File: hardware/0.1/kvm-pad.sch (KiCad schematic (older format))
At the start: 50 parts, among them J1 USB_C_Receptacle_USB2.0, J2 USB_C_Receptacle_USB2.0, J3 AVR-ISP-6, K1 KEYSW, K2 KEYSW, K3 KEYSW, K4 KEYSW, K5 KEYSW, K6 KEYSW, K7 KEYSW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

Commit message: [sch][pcb] Swap USBLC6 IOs for easing PCB routing
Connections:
- net 1_D+: now also U1.1 (IO1); no longer U1.3 (IO2)
- net 1_D-: now also U1.3 (IO2); no longer U1.1 (IO1)
- net 2_D+: now also U3.1 (IO1); no longer U3.3 (IO2)
- net 2_D-: now also U3.3 (IO2); no longer U3.1 (IO1)
- net USB_1_D+: now also U1.6 (IO1); no longer U1.4 (IO2)
- net USB_1_D-: now also U1.4 (IO2); no longer U1.6 (IO1)
- net USB_2_D+: now also U3.6 (IO1); no longer U3.4 (IO2)
- net USB_2_D-: now also U3.4 (IO2); no longer U3.6 (IO1)
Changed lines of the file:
@@
 	1700 1950 1650 1950
 Wire Wire Line
-	1700 1700 2150 1700
+	1700 1700 2150 1900
 Connection ~ 1700 1700
 Wire Wire Line
 	1700 1700 1700 1750
-Text Label 2150 1700 2    50   ~ 0
+Text Label 2150 1900 2    50   ~ 0
 1_D-
 Wire Wire Line
-	1700 1900 2150 1900
+	1700 1900 2150 1700
 Connection ~ 1700 1900
 Wire Wire Line
@@
 	1650 4100 1700 4100
 Wire Wire Line
-	1700 4100 1700 4150
-Wire Wire Line
 	1700 4200 1650 4200
 Wire Wire Line
-	1700 3950 2150 3950
+	1700 3950 2150 4150
 Connection ~ 1700 3950
 Wire Wire Line
 	1700 3950 1700 4000
-Wire Wire Line
-	1700 4150 2150 4150
-Connection ~ 1700 4150
-Wire Wire Line
-	1700 4150 1700 4200
 $Comp
 L josh-passive:RN RN?
@@
 	1    0    0    -1
 $EndComp
-Text Label 2150 1900 2    50   ~ 0
+Text Label 2150 1700 2    50   ~ 0
 1_D+
+Text Label 2150 3950 2    50   ~ 0
+2_D+
 Text Label 2150 4150 2    50   ~ 0
-2_D+
-Text Label 2150 3950 2    50   ~ 0
 2_D-
 $Comp
@@
 Wire Wire Line
 	2350 1150 2550 1150
+Text Label 3400 1700 2    50   ~ 0
+USB_1_D+
+Wire Wire Line
+	2950 1900 3400 1900
 Text Label 3400 1900 2    50   ~ 0
-USB_1_D+
-Wire Wire Line
-	2950 1900 3400 1900
-Text Label 3400 1700 2    50   ~ 0
 USB_1_D-
 Wire Wire Line
@@
 Wire Wire Line
 	2950 4150 3400 4150
+Text Label 3400 3950 2    50   ~ 0
+USB_2_D+
 Text Label 3400 4150 2    50   ~ 0
-USB_2_D+
-Text Label 3400 3950 2    50   ~ 0
 USB_2_D-
 Text Notes 1100 5525 0    100  ~ 0
@@
 	1    0    0    -1
 $EndComp
+Wire Wire Line
+	1700 4100 1700 4150
+Wire Wire Line
+	1700 4150 2150 3950
+Connection ~ 1700 4150
+Wire Wire Line
+	1700 4150 1700 4200
 $EndSCHEMATC

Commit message: [pcb] Switch RN1 to 4xR
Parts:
- R17, R18, R19, R20: renamed from RN1; footprint Resistor_SMD:R_Array_Convex_4x0603 -> Resistor_SMD:R_0603_1608Metric; symbol josh-passive:RN -> Device:R
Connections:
- net GND: now also R17.1, R18.1, R19.1, R20.1; no longer R17.5, R18.6, R19.7, R20.8
- net at J1.A5 (CC1): now also R17.2; no longer R17.4
- net at J1.B5 (CC2): now also R18.2; no longer R18.3
- net at J2.B5 (CC2): now also R20.2; no longer R20.1
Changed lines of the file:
@@
 	0    1    1    0
-$EndComp
-$Comp
-L josh-passive:RN RN?
-U 1 1 603A219F
-P 1850 1350
-AR Path="/5EDC3803/603A219F" Ref="RN?"  Part="1"
-AR Path="/603A219F" Ref="RN1"  Part="1"
-F 0 "RN1" H 1850 1450 50  0000 C CNN
-F 1 "5K1" H 1850 1350 50  0000 C CNN
-F 2 "Resistor_SMD:R_Array_Convex_4x0603" V 1850 1350 50  0001 C CNN
-F 3 "~" V 1850 1350 50  0001 C CNN
-	1    1850 1350
-	1    0    0    -1
-$EndComp
-$Comp
-L josh-passive:RN RN?
-U 2 1 603A21A5
-P 1850 1450
-AR Path="/5EDC3803/603A21A5" Ref="RN?"  Part="2"
-AR Path="/603A21A5" Ref="RN1"  Part="2"
-F 0 "RN1" H 1850 1350 50  0000 C CNN
-F 1 "5K1" H 1850 1450 50  0000 C CNN
-F 2 "Resistor_SMD:R_Array_Convex_4x0603" V 1850 1450 50  0001 C CNN
-F 3 "~" V 1850 1450 50  0001 C CNN
-	2    1850 1450
-	1    0    0    -1
 $EndComp
 Wire Wire Line
@@
 Wire Wire Line
 	1700 3950 1700 4000
-$Comp
-L josh-passive:RN RN?
-U 3 1 603A21FB
-P 1850 3600
-AR Path="/5EDC3803/603A21FB" Ref="RN?"  Part="3"
-AR Path="/603A21FB" Ref="RN1"  Part="3"
-F 0 "RN1" H 1850 3700 50  0000 C CNN
-F 1 "5K1" H 1850 3600 50  0000 C CNN
-F 2 "Resistor_SMD:R_Array_Convex_4x0603" V 1850 3600 50  0001 C CNN
-F 3 "~" V 1850 3600 50  0001 C CNN
-	3    1850 3600
-	1    0    0    -1
-$EndComp
-$Comp
-L josh-passive:RN RN?
-U 4 1 603A2201
-P 1850 3700
-AR Path="/5EDC3803/603A2201" Ref="RN?"  Part="4"
-AR Path="/603A2201" Ref="RN1"  Part="4"
-F 0 "RN1" H 1850 3600 50  0000 C CNN
-F 1 "5K1" H 1850 3700 50  0000 C CNN
-F 2 "Resistor_SMD:R_Array_Convex_4x0603" V 1850 3700 50  0001 C CNN
-F 3 "~" V 1850 3700 50  0001 C CNN
-	4    1850 3700
-	1    0    0    -1
-$EndComp
 Wire Wire Line
 	1700 3700 1650 3700
-Wire Wire Line
-	1650 3600 1700 3600
 Wire Wire Line
 	2000 3600 2050 3600
@@
 Text Notes 1100 5525 0    100  ~ 0
 USB Switch and Hub
-$Comp
-L Connector:USB_C_Receptacle_USB2.0 J?
-U 1 1 603A2178
-P 1050 1750
-AR Path="/5EDC3803/603A2178" Ref="J?"  Part="1"
-AR Path="/603A2178" Ref="J1"  Part="1"
-F 0 "J1" H 1157 2617 50  0000 C CNN
-F 1 "USB_C_Receptacle_USB2.0" H 1157 2526 50  0000 C CNN
-F 2 "josh-connectors:USB_C_U262-161N-4BVC11" H 1200 1750 50  0001 C CNN
-F 3 "https://www.usb.org/sites/default/files/documents/usb_type-c.zip" H 1200 1750 50  0001 C CNN
-	1    1050 1750
-	1    0    0    -1
-$EndComp
 $Comp
 L Connector:USB_C_Receptacle_USB2.0 J?
@@
 Wire Wire Line
 	1700 4150 1700 4200
+$Comp
+L Connector:USB_C_Receptacle_USB2.0 J?
+U 1 1 603A2178
+P 1050 1750
+AR Path="/5EDC3803/603A2178" Ref="J?"  Part="1"
+AR Path="/603A2178" Ref="J1"  Part="1"
+F 0 "J1" H 1157 2617 50  0000 C CNN
+F 1 "USB_C_Receptacle_USB2.0" H 1157 2526 50  0000 C CNN
+F 2 "josh-connectors:USB_C_U262-161N-4BVC11" H 1200 1750 50  0001 C CNN
+F 3 "https://www.usb.org/sites/default/files/documents/usb_type-c.zip" H 1200 1750 50  0001 C CNN
+	1    1050 1750
+	1    0    0    -1
+$EndComp
+Wire Wire Line
+	1650 3600 1700 3600
+$Comp
+L Device:R RN?
+U 1 1 603A2201
+P 1850 3700
+AR Path="/5EDC3803/603A2201" Ref="RN?"  Part="4"
+AR Path="/603A2201" Ref="R20"  Part="1"
+F 0 "R20" V 1950 3700 50  0000 C CNN
+F 1 "5K1" V 1850 3700 50  0000 C CNN
+F 2 "Resistor_SMD:R_0603_1608Metric" V 1850 3700 50  0001 C CNN
+F 3 "~" V 1850 3700 50  0001 C CNN
+	1    1850 3700
+	0    1    1    0
+$EndComp
+$Comp
+L Device:R RN?
+U 1 1 603A21A5
+P 1850 1450
+AR Path="/5EDC3803/603A21A5" Ref="RN?"  Part="2"
+AR Path="/603A21A5" Ref="R18"  Part="1"
+F 0 "R18" V 1950 1450 50  0000 C CNN
+F 1 "5K1" V 1850 1450 50  0000 C CNN
+F 2 "Resistor_SMD:R_0603_1608Metric" V 1850 1450 50  0001 C CNN
+F 3 "~" V 1850 1450 50  0001 C CNN
+	1    1850 1450
+	0    1    1    0
+$EndComp
+$Comp
+L Device:R RN?
+U 1 1 603A219F
+P 1850 1350
+AR Path="/5EDC3803/603A219F" Ref="RN?"  Part="1"
+AR Path="/603A219F" Ref="R17"  Part="1"
+F 0 "R17" V 1750 1350 50  0000 C CNN
+F 1 "5K1" V 1850 1350 50  0000 C CNN
+F 2 "Resistor_SMD:R_0603_1608Metric" V 1850 1350 50  0001 C CNN
+F 3 "~" V 1850 1350 50  0001 C CNN
+	1    1850 1350
+	0    1    1    0
+$EndComp
+$Comp
+L Device:R RN?
+U 1 1 603A21FB
+P 1850 3600
+AR Path="/5EDC3803/603A21FB" Ref="RN?"  Part="3"
+AR Path="/603A21FB" Ref="R19"  Part="1"
+F 0 "R19" V 1750 3600 50  0000 C CNN
+F 1 "5K1" V 1850 3600 50  0000 C CNN
+F 2 "Resistor_SMD:R_0603_1608Metric" V 1850 3600 50  0001 C CNN
+F 3 "~" V 1850 3600 50  0001 C CNN
+	1    1850 3600
+	0    1    1    0
+$EndComp
 $EndSCHEMATC

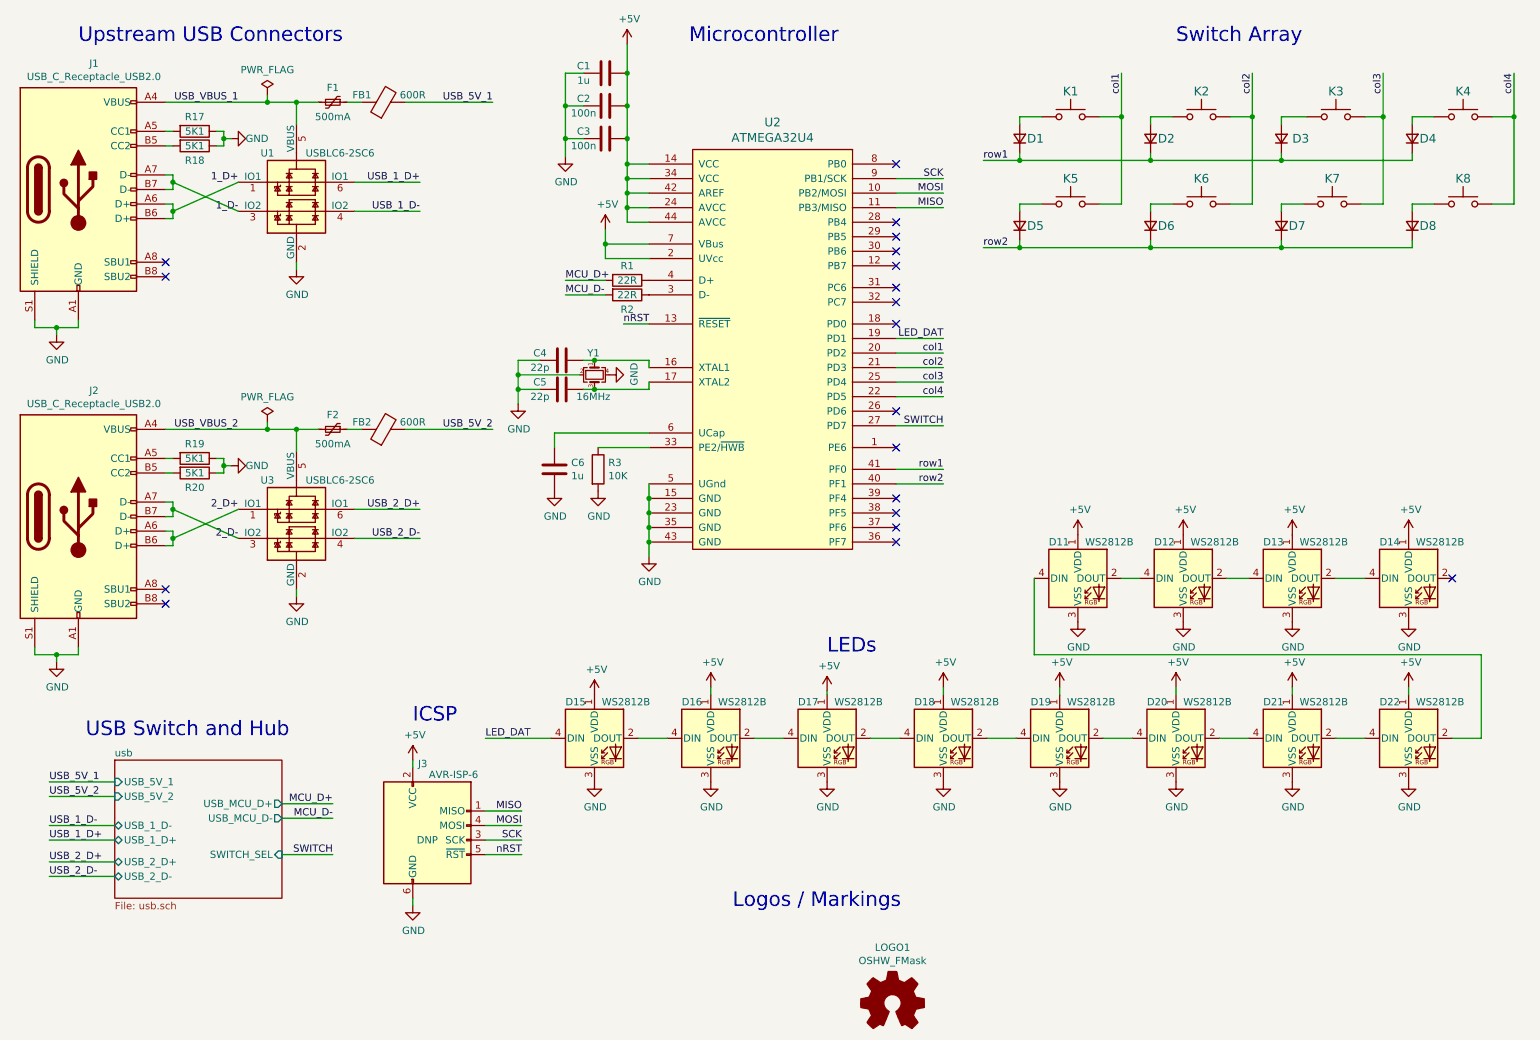
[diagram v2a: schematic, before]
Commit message: alt layout
following what usb says... ;p
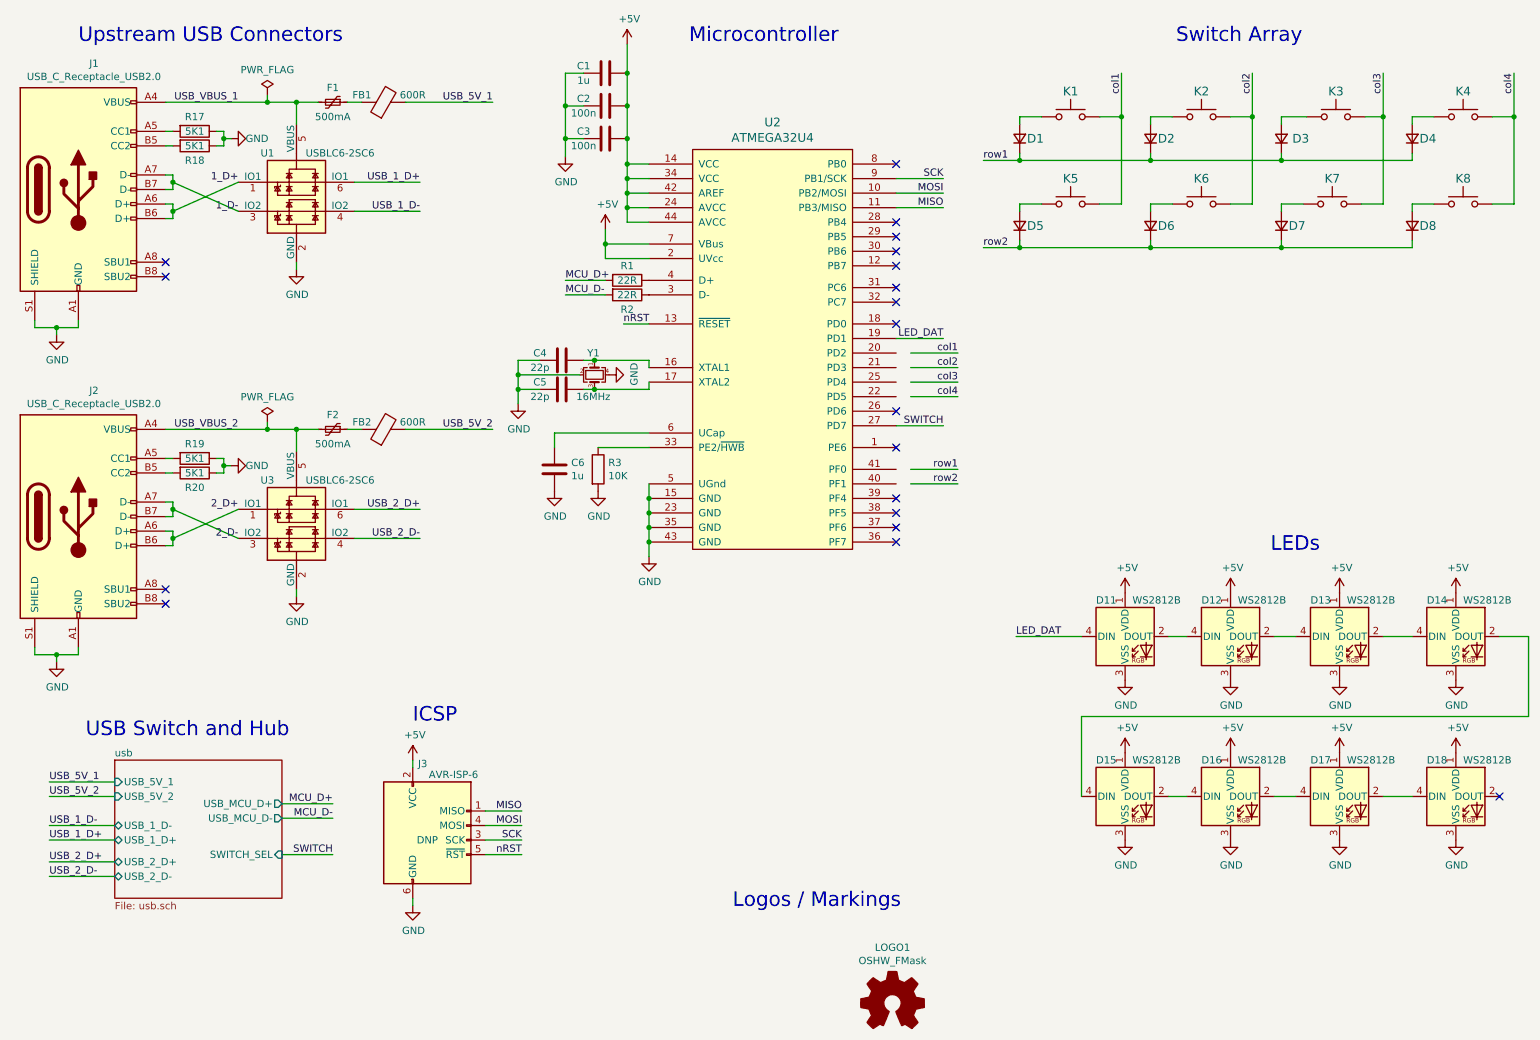
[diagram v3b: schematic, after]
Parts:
- removed D19, D20, D21, D22: WS2812B, josh-led:SK8612-MINI-E, symbol LED:WS2812B
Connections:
- wire segments 206 -> 195
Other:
- moved on the sheet: D11, D12, D13, D14, D15, D16, D17, D18
